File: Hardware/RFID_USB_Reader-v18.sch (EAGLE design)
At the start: 26 parts, among them Q1 MMBT2222, U1 ID-12/20SMD, U5 CH340C

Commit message: post checklist changes
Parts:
- removed U$2: CREATIVE_COMMONS, SparkFun:CREATIVE_COMMONS
- added FRAME1: FRAME-LETTER, SparkFun-Aesthetics:FRAME-LETTER
- added JP1, JP5: FIDUCIAL1X2, SparkFun:FIDUCIAL1X2
- added LOGO4: REVISION, SparkFun-Aesthetics:REVISION
- LED1: value GREEN -> BLUE; device SparkFun-LED:LED-GREEN0603 -> SparkFun-LED:LED-BLUE0603
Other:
- note added: "A. England"
- note added: "A. Weiss"
- note added: "Buzzer / Indicator LED"
- note added: "PTH Connections"
- note added: "RFID Reader"
- note added: "USB-C to Serial"
- note added: "VIN: 2.8-5V"
- note added: "v13"
- note removed: "A.Weiss"
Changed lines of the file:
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@@
 </classes>
 <parts>
-<part name="LED1" library="SparkFun-LED" deviceset="LED-GREEN" device="0603" value="GREEN"/>
+<part name="LED1" library="SparkFun-LED" deviceset="LED-BLUE" device="0603" value="BLUE"/>
 <part name="R1" library="SparkFun-Resistors" deviceset="330OHM" device="-0603-1/10W-1%" value="330"/>
 <part name="P+2" library="SparkFun" deviceset="VCC" device=""/>
@@
 <part name="P+4" library="SparkFun" deviceset="VCC" device=""/>
 <part name="GND6" library="SparkFun" deviceset="GND" device=""/>
-<part name="FRAME1" library="SparkFun" deviceset="FRAME-LETTER" device=""/>
+<part name="FRAME1" library="SparkFun-Aesthetics" deviceset="FRAME-LETTER" device=""/>
 <part name="U$4" library="SparkFun" deviceset="STAND-OFF" device=""/>
 <part name="U$5" library="SparkFun" deviceset="STAND-OFF" device=""/>
@@
 <part name="GND7" library="SparkFun" deviceset="GND" device=""/>
 <part name="SG1" library="SparkFun" deviceset="BUZZER" device="SMD2"/>
-<part name="U$2" library="SparkFun" deviceset="CREATIVE_COMMONS" device=""/>
 <part name="BUZZ" library="SparkFun-Jumpers" deviceset="JUMPER-SMT_2_NO" device="_NO-SILK" package3d_urn="urn:adsk.eagle:package:39277/1" value="buzz"/>
 <part name="JP2" library="SparkFun" deviceset="FIDUCIAL" device="1X2"/>
@@
 <part name="LOGO2" library="SparkFun-Aesthetics" deviceset="SFE_LOGO_NAME_FLAME" device=".1_INCH"/>
 <part name="LOGO3" library="SparkFun-Aesthetics" deviceset="OSHW-LOGO" device="S"/>
+<part name="LOGO4" library="SparkFun-Aesthetics" deviceset="REVISION" device=""/>
+<part name="JP1" library="SparkFun" deviceset="FIDUCIAL" device="1X2"/>
+<part name="JP5" library="SparkFun" deviceset="FIDUCIAL" device="1X2"/>
 </parts>
 <sheets>
@@
 <wire x1="0" y1="101.6" x2="248.92" y2="101.6" width="0.2032" layer="95" style="shortdash"/>
 <wire x1="147.32" y1="185.42" x2="147.32" y2="35.56" width="0.2032" layer="95" style="shortdash"/>
-<text x="38.1" y="10.16" size="1.778" layer="97">A.Weiss</text>
+<text x="166.116" y="11.43" size="2.54" layer="94" font="vector">A. Weiss</text>
+<text x="169.164" y="7.112" size="2.54" layer="94" font="vector">A. England</text>
+<text x="236.22" y="7.62" size="2.54" layer="94" font="vector">v13</text>
+<text x="2.54" y="96.52" size="2.54" layer="94" font="vector">RFID Reader</text>
+<text x="2.54" y="180.34" size="2.54" layer="94" font="vector">USB-C to Serial</text>
+<text x="149.86" y="180.34" size="2.54" layer="94" font="vector">Buzzer / Indicator LED</text>
+<text x="149.86" y="96.52" size="2.54" layer="94" font="vector">PTH Connections</text>
+<text x="2.54" y="93.98" size="1.778" layer="94" font="vector">VIN: 2.8-5V</text>
 </plain>
 <instances>
@@
 <instance part="GND6" gate="1" x="88.9" y="45.72"/>
 <instance part="FRAME1" gate="G$1" x="0" y="0"/>
-<instance part="FRAME1" gate="G$2" x="147.32" y="0"/>
+<instance part="FRAME1" gate="V" x="147.32" y="0"/>
 <instance part="U$4" gate="G$1" x="236.22" y="27.94"/>
 <instance part="U$5" gate="G$1" x="231.14" y="27.94"/>
@@
 <attribute name="VALUE" x="208.28" y="146.05" size="1.27" layer="96" rot="R270"/>
 </instance>
-<instance part="U$2" gate="G$1" x="20.32" y="10.16"/>
 <instance part="BUZZ" gate="G$1" x="198.12" y="154.94" rot="R90"/>
-<instance part="JP2" gate="G$1" x="157.48" y="27.94"/>
-<instance part="JP3" gate="G$1" x="162.56" y="27.94"/>
+<instance part="JP2" gate="G$1" x="226.06" y="30.48"/>
+<instance part="JP3" gate="G$1" x="220.98" y="30.48"/>
 <instance part="U5" gate="U1" x="106.68" y="147.32"/>
 <instance part="J10" gate="J1" x="45.72" y="147.32"/>
@@
 <instance part="LOGO2" gate="G$1" x="88.9" y="2.54"/>
 <instance part="LOGO3" gate="G$1" x="236.22" y="45.72"/>
+<instance part="LOGO4" gate="G$1" x="148.844" y="7.112"/>
+<instance part="JP1" gate="G$1" x="231.14" y="30.48"/>
+<instance part="JP5" gate="G$1" x="236.22" y="30.48"/>
 </instances>
 <busses>

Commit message: post review changes
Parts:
- removed J2: (no value), SparkFun-Connectors:CONN_05NO_SILK
- added J1: (no value), SparkFun-Connectors:CONN_07
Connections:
- net LED renamed INDICATOR
- new net ANT1: J1.3, U1.ANT1
- new net ANT2: J1.2, U1.ANT2
- net CP: now also J1.1; no longer J2.1
- net GND: now also J1.6; no longer J2.4
- net TX-O: now also J1.5; no longer J2.3
- net TX-O-RS232: now also J1.4; no longer J2.2
- net VCC: now also J1.7; no longer J2.5
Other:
- note added: "VCC: 2.8-5V"
- note removed: "VIN: 2.8-5V"
- moved on the sheet: SG1
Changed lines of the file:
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@@
 <part name="U1" library="SparkFun-RF" deviceset="ID-12/20" device="SMD"/>
 <part name="C1" library="SparkFun-Capacitors" deviceset="2.2UF" device="-0603-10V-20%" value="2.2uF"/>
-<part name="J2" library="SparkFun-Connectors" deviceset="CONN_05" device="NO_SILK"/>
 <part name="LOGO1" library="SparkFun-Aesthetics" deviceset="SFE_LOGO_NAME_FLAME" device=".1_INCH"/>
 <part name="LOGO2" library="SparkFun-Aesthetics" deviceset="SFE_LOGO_NAME_FLAME" device=".1_INCH"/>
@@
 <part name="JP1" library="SparkFun" deviceset="FIDUCIAL" device="1X2"/>
 <part name="JP5" library="SparkFun" deviceset="FIDUCIAL" device="1X2"/>
+<part name="J1" library="SparkFun-Connectors" deviceset="CONN_07" device=""/>
 </parts>
 <sheets>
@@
 <text x="149.86" y="180.34" size="2.54" layer="94" font="vector">Buzzer / Indicator LED</text>
 <text x="149.86" y="96.52" size="2.54" layer="94" font="vector">PTH Connections</text>
-<text x="2.54" y="93.98" size="1.778" layer="94" font="vector">VIN: 2.8-5V</text>
+<text x="2.54" y="93.98" size="1.778" layer="94" font="vector">VCC: 2.8-5V</text>
 </plain>
 <instances>
@@
 <instance part="R2" gate="G$1" x="180.34" y="121.92"/>
 <instance part="GND7" gate="1" x="193.04" y="111.76"/>
-<instance part="SG1" gate="G$1" x="200.66" y="142.24" smashed="yes" rot="R270">
-<attribute name="NAME" x="205.74" y="144.78" size="1.27" layer="95" rot="R270"/>
-<attribute name="VALUE" x="208.28" y="146.05" size="1.27" layer="96" rot="R270"/>
+<instance part="SG1" gate="G$1" x="203.2" y="142.24" smashed="yes" rot="R270">
+<attribute name="NAME" x="208.28" y="144.78" size="1.27" layer="95" rot="R270"/>
+<attribute name="VALUE" x="210.82" y="146.05" size="1.27" layer="96" rot="R270"/>
 </instance>
 <instance part="BUZZ" gate="G$1" x="198.12" y="154.94" rot="R90"/>
@@
 <instance part="P+5" gate="1" x="27.94" y="157.48"/>
 <instance part="GND1" gate="1" x="193.04" y="60.96"/>
-<instance part="P+6" gate="1" x="193.04" y="78.74"/>
+<instance part="P+6" gate="1" x="193.04" y="83.82"/>
 <instance part="U1" gate="G$1" x="73.66" y="60.96"/>
 <instance part="C1" gate="G$1" x="73.66" y="76.2" rot="R90"/>
-<instance part="J2" gate="G$1" x="182.88" y="71.12"/>
 <instance part="LOGO1" gate="G$1" x="88.9" y="2.54"/>
 <instance part="LOGO2" gate="G$1" x="88.9" y="2.54"/>
@@
 <instance part="JP1" gate="G$1" x="231.14" y="30.48"/>
 <instance part="JP5" gate="G$1" x="236.22" y="30.48"/>
+<instance part="J1" gate="J1" x="185.42" y="71.12"/>
 </instances>
 <busses>
@@
 </segment>
 <segment>
-<wire x1="190.5" y1="73.66" x2="193.04" y2="73.66" width="0.1524" layer="91"/>
+<wire x1="190.5" y1="78.74" x2="193.04" y2="78.74" width="0.1524" layer="91"/>
 <pinref part="GND1" gate="1" pin="GND"/>
-<wire x1="193.04" y1="63.5" x2="193.04" y2="73.66" width="0.1524" layer="91"/>
-<pinref part="J2" gate="G$1" pin="4"/>
+<wire x1="193.04" y1="63.5" x2="193.04" y2="78.74" width="0.1524" layer="91"/>
+<pinref part="J1" gate="J1" pin="6"/>
 </segment>
 <segment>
@@
 </segment>
 <segment>
-<wire x1="190.5" y1="76.2" x2="193.04" y2="76.2" width="0.1524" layer="91"/>
+<wire x1="190.5" y1="81.28" x2="193.04" y2="81.28" width="0.1524" layer="91"/>
 <pinref part="P+6" gate="1" pin="VCC"/>
-<wire x1="193.04" y1="78.74" x2="193.04" y2="76.2" width="0.1524" layer="91"/>
-<pinref part="J2" gate="G$1" pin="5"/>
+<wire x1="193.04" y1="83.82" x2="193.04" y2="81.28" width="0.1524" layer="91"/>
+<pinref part="J1" gate="J1" pin="7"/>
 </segment>
 <segment>
@@
 </segment>
 <segment>
-<wire x1="190.5" y1="71.12" x2="195.58" y2="71.12" width="0.1524" layer="91"/>
-<label x="195.58" y="71.12" size="1.27" layer="95" xref="yes"/>
-<pinref part="J2" gate="G$1" pin="3"/>
-</segment>
-<segment>
 <pinref part="U5" gate="U1" pin="RXI"/>
 <wire x1="116.84" y1="152.4" x2="119.38" y2="152.4" width="0.1524" layer="91"/>
 <label x="119.38" y="152.4" size="1.27" layer="95" font="vector" xref="yes"/>
 </segment>
+<segment>
+<wire x1="190.5" y1="76.2" x2="195.58" y2="76.2" width="0.1524" layer="91"/>
+<pinref part="J1" gate="J1" pin="5"/>
+<label x="195.58" y="76.2" size="1.27" layer="95" font="vector" xref="yes"/>
+</segment>
 </net>
 <net name="TX-O-RS232" class="0">
@@
 </segment>
 <segment>
-<wire x1="190.5" y1="68.58" x2="195.58" y2="68.58" width="0.1524" layer="91"/>
-<label x="195.58" y="68.58" size="1.27" layer="95" xref="yes"/>
-<pinref part="J2" gate="G$1" pin="2"/>
-</segment>
-</net>
-<net name="LED" class="0">
+<wire x1="190.5" y1="73.66" x2="195.58" y2="73.66" width="0.1524" layer="91"/>
+<pinref part="J1" gate="J1" pin="4"/>
+<label x="195.58" y="73.66" size="1.27" layer="95" font="vector" xref="yes"/>
+</segment>
+</net>
+<net name="INDICATOR" class="0">
 <segment>
 <wire x1="86.36" y1="63.5" x2="88.9" y2="63.5" width="0.1524" layer="91"/>
@@
 <wire x1="190.5" y1="66.04" x2="195.58" y2="66.04" width="0.1524" layer="91"/>
 <label x="195.58" y="66.04" size="1.27" layer="95" xref="yes"/>
-<pinref part="J2" gate="G$1" pin="1"/>
+<pinref part="J1" gate="J1" pin="1"/>
 </segment>
 </net>
@@
 <wire x1="187.96" y1="129.54" x2="187.96" y2="132.08" width="0.1524" layer="91"/>
 <wire x1="193.04" y1="127" x2="193.04" y2="129.54" width="0.1524" layer="91"/>
-<wire x1="198.12" y1="139.7" x2="198.12" y2="129.54" width="0.1524" layer="91"/>
 <junction x="193.04" y="129.54"/>
-<pinref part="SG1" gate="G$1" pin="2"/>
 <pinref part="R1" gate="G$1" pin="1"/>
 <pinref part="Q1" gate="G$1" pin="C"/>
+<pinref part="SG1" gate="G$1" pin="2"/>
+<wire x1="200.66" y1="139.7" x2="198.12" y2="139.7" width="0.1524" layer="91"/>
+<wire x1="198.12" y1="139.7" x2="198.12" y2="129.54" width="0.1524" layer="91"/>
 </segment>
 </net>
@@
 <pinref part="Q1" gate="G$1" pin="B"/>
 <pinref part="R2" gate="G$1" pin="2"/>
-</segment>
-</net>
-<net name="N$5" class="0">
-<segment>
-<wire x1="198.12" y1="142.24" x2="198.12" y2="149.86" width="0.1524" layer="91"/>
-<pinref part="SG1" gate="G$1" pin="1"/>
-<pinref part="BUZZ" gate="G$1" pin="1"/>
 </segment>
 </net>
@@
 </segment>
 </net>
+<net name="N$4" class="0">
+<segment>
+<pinref part="BUZZ" gate="G$1" pin="1"/>
+<wire x1="198.12" y1="149.86" x2="198.12" y2="142.24" width="0.1524" layer="91"/>
+<pinref part="SG1" gate="G$1" pin="1"/>
+<wire x1="198.12" y1="142.24" x2="200.66" y2="142.24" width="0.1524" layer="91"/>
+</segment>
+</net>
+<net name="ANT1" class="0">
+<segment>
+<pinref part="U1" gate="G$1" pin="ANT1"/>
+<wire x1="60.96" y1="58.42" x2="58.42" y2="58.42" width="0.1524" layer="91"/>
+<label x="58.42" y="58.42" size="1.27" layer="95" font="vector" rot="R180" xref="yes"/>
+</segment>
+<segment>
+<wire x1="190.5" y1="71.12" x2="195.58" y2="71.12" width="0.1524" layer="91"/>
+<label x="195.58" y="71.12" size="1.27" layer="95" xref="yes"/>
+<pinref part="J1" gate="J1" pin="3"/>
+</segment>
+</net>
+<net name="ANT2" class="0">
+<segment>
+<pinref part="U1" gate="G$1" pin="ANT2"/>
+<wire x1="60.96" y1="55.88" x2="58.42" y2="55.88" width="0.1524" layer="91"/>
+<label x="58.42" y="55.88" size="1.27" layer="95" font="vector" rot="R180" xref="yes"/>
+</segment>
+<segment>
+<wire x1="190.5" y1="68.58" x2="195.58" y2="68.58" width="0.1524" layer="91"/>
+<label x="195.58" y="68.58" size="1.27" layer="95" xref="yes"/>
+<pinref part="J1" gate="J1" pin="2"/>
+</segment>
+</net>

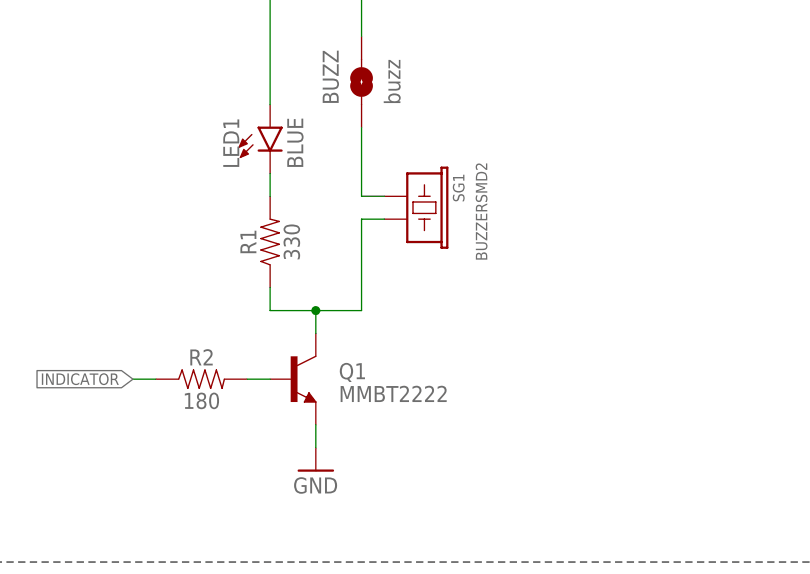
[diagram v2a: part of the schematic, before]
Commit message: updating Buzzer and npn transistor to have PROD_ID
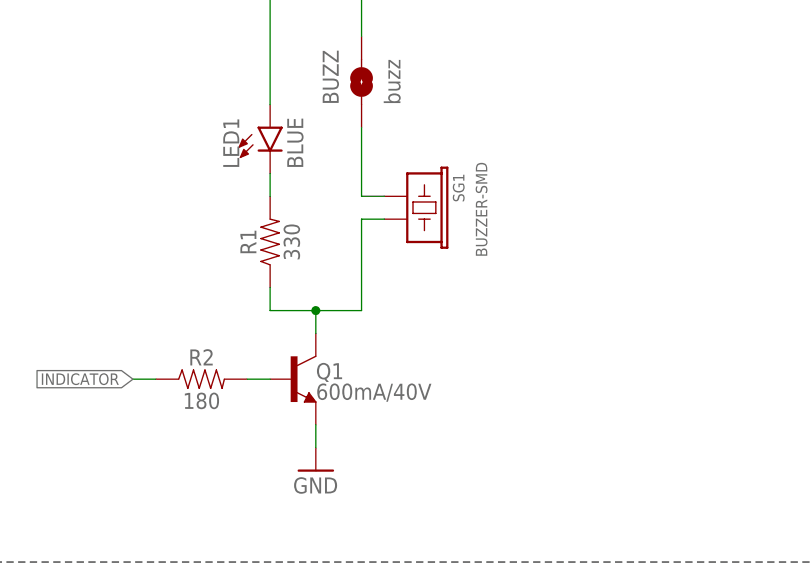
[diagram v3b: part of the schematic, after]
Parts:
- Q1: value MMBT2222 -> 600mA/40V; device SparkFun:TRANSISTOR_NPNSOT23-3 -> SparkFun-DiscreteSemi:TRANS_NPN-MMBT2222AL
- SG1: value BUZZERSMD2 -> BUZZER-SMD; device SparkFun:BUZZERSMD2 -> SparkFun-Electromechanical:BUZZER-SMD
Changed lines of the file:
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@@
 <part name="U$6" library="SparkFun" deviceset="STAND-OFF" device=""/>
 <part name="U$7" library="SparkFun" deviceset="STAND-OFF" device=""/>
-<part name="Q1" library="SparkFun" deviceset="TRANSISTOR_NPN" device="SOT23-3" value="MMBT2222"/>
+<part name="Q1" library="SparkFun-DiscreteSemi" deviceset="TRANS_NPN" device="-MMBT2222AL" value="600mA/40V"/>
 <part name="R2" library="SparkFun-Resistors" deviceset="180OHM" device="-0603-1/10W-1%" value="180"/>
 <part name="GND7" library="SparkFun" deviceset="GND" device=""/>
-<part name="SG1" library="SparkFun" deviceset="BUZZER" device="SMD2"/>
+<part name="SG1" library="SparkFun-Electromechanical" deviceset="BUZZER" device="-SMD"/>
 <part name="BUZZ" library="SparkFun-Jumpers" deviceset="JUMPER-SMT_2_NO" device="_NO-SILK" package3d_urn="urn:adsk.eagle:package:39277/1" value="buzz"/>
 <part name="JP2" library="SparkFun" deviceset="FIDUCIAL" device="1X2"/>
